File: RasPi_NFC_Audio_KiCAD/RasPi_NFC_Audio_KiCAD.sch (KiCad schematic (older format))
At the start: 21 parts, among them J1 Barrel_Jack_Switch, J2 Conn_02x20_Odd_Even, J3 Connector_01x10, U1 MIC5225-3.3V

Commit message: Layout updates
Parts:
- J2: footprint Connector_PinSocket_2.54mm:PinSocket_2x20_P2.54mm_Vertical -> Connector_PinHeader_2.54mm:PinHeader_2x20_P2.54mm_Vertical
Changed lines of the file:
@@
 EESchema Schematic File Version 4
 LIBS:RasPi_NFC_Audio_KiCAD-cache
-EELAYER 30 0
+EELAYER 29 0
 EELAYER END
 $Descr A4 11693 8268
@@
 F 0 "J2" H 4130 6450 50  0000 C CNN
 F 1 "Conn_02x20_Odd_Even" H 4140 6416 50  0001 C CNN
-F 2 "Connector_PinSocket_2.54mm:PinSocket_2x20_P2.54mm_Vertical" H -760 4440 50  0001 C CNN
+F 2 "Connector_PinHeader_2.54mm:PinHeader_2x20_P2.54mm_Vertical" H -760 4440 50  0001 C CNN
 F 3 "" H -760 4440 50  0001 C CNN
 F 4 "M20-7831046" H 4090 5390 50  0001 C CNN "Part #"

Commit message: Layout updates
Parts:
- added C28: 100u, Capacitor_SMD:C_1206_3216Metric_Pad1.42x1.75mm_HandSolder, symbol Device:C
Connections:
- net +5V: now also C28.1
- net GND: now also C28.2
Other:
- moved on the sheet: C1, C2, TP2
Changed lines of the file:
@@
 EESchema Schematic File Version 4
 LIBS:RasPi_NFC_Audio_KiCAD-cache
-EELAYER 29 0
+EELAYER 30 0
 EELAYER END
 $Descr A4 11693 8268
@@
 L Device:C C1
 U 1 1 5E1A86EE
-P 2060 2330
-F 0 "C1" H 2175 2376 50  0000 L CNN
-F 1 "100u" H 2175 2285 50  0000 L CNN
-F 2 "Capacitor_SMD:C_1206_3216Metric_Pad1.42x1.75mm_HandSolder" H 2098 2180 50  0001 C CNN
-F 3 "~" H 2060 2330 50  0001 C CNN
-F 4 "GRM31CD80J107ME39L" H 2060 2330 50  0001 C CNN "Part #"
-F 5 "490-10525-1-ND" H 2060 2330 50  0001 C CNN "DigiKey"
-	1    2060 2330
+P 1960 2330
+F 0 "C1" H 2000 2420 50  0000 L CNN
+F 1 "100u" H 1990 2230 50  0000 L CNN
+F 2 "Capacitor_SMD:C_1206_3216Metric_Pad1.42x1.75mm_HandSolder" H 1998 2180 50  0001 C CNN
+F 3 "~" H 1960 2330 50  0001 C CNN
+F 4 "GRM31CD80J107ME39L" H 1960 2330 50  0001 C CNN "Part #"
+F 5 "490-10525-1-ND" H 1960 2330 50  0001 C CNN "DigiKey"
+	1    1960 2330
 	1    0    0    -1
 $EndComp
@@
 L Device:C C2
 U 1 1 5E1AABBB
-P 2510 2330
-F 0 "C2" H 2625 2376 50  0000 L CNN
-F 1 "10u" H 2625 2285 50  0000 L CNN
-F 2 "Capacitor_SMD:C_0603_1608Metric_Pad1.05x0.95mm_HandSolder" H 2548 2180 50  0001 C CNN
-F 3 "~" H 2510 2330 50  0001 C CNN
-F 4 "CL10A106MQ8NNNC" H 2510 2330 50  0001 C CNN "Part #"
-F 5 "1276-1119-1-ND" H 2510 2330 50  0001 C CNN "DigiKey"
-	1    2510 2330
+P 2650 2330
+F 0 "C2" H 2680 2410 50  0000 L CNN
+F 1 "10u" H 2680 2240 50  0000 L CNN
+F 2 "Capacitor_SMD:C_0603_1608Metric_Pad1.05x0.95mm_HandSolder" H 2688 2180 50  0001 C CNN
+F 3 "~" H 2650 2330 50  0001 C CNN
+F 4 "CL10A106MQ8NNNC" H 2650 2330 50  0001 C CNN "Part #"
+F 5 "1276-1119-1-ND" H 2650 2330 50  0001 C CNN "DigiKey"
+	1    2650 2330
 	1    0    0    -1
 $EndComp
@@
 L power:GND #PWR0102
 U 1 1 5E1B33E8
-P 2060 2550
-F 0 "#PWR0102" H 2060 2300 50  0001 C CNN
-F 1 "GND" H 2060 2400 50  0000 C CNN
-F 2 "" H 2060 2550 50  0000 C CNN
-F 3 "" H 2060 2550 50  0000 C CNN
-	1    2060 2550
+P 1960 2550
+F 0 "#PWR0102" H 1960 2300 50  0001 C CNN
+F 1 "GND" H 1960 2400 50  0000 C CNN
+F 2 "" H 1960 2550 50  0000 C CNN
+F 3 "" H 1960 2550 50  0000 C CNN
+	1    1960 2550
 	1    0    0    -1
 $EndComp
@@
 L power:GND #PWR0103
 U 1 1 5E1B3827
-P 2510 2550
-F 0 "#PWR0103" H 2510 2300 50  0001 C CNN
-F 1 "GND" H 2510 2400 50  0000 C CNN
-F 2 "" H 2510 2550 50  0000 C CNN
-F 3 "" H 2510 2550 50  0000 C CNN
-	1    2510 2550
-	1    0    0    -1
-$EndComp
-Wire Wire Line
-	2060 2550 2060 2480
-Wire Wire Line
-	2510 2550 2510 2480
-Wire Wire Line
-	2060 2180 2060 2120
-Wire Wire Line
-	2510 2180 2510 2120
+P 2650 2550
+F 0 "#PWR0103" H 2650 2300 50  0001 C CNN
+F 1 "GND" H 2650 2400 50  0000 C CNN
+F 2 "" H 2650 2550 50  0000 C CNN
+F 3 "" H 2650 2550 50  0000 C CNN
+	1    2650 2550
+	1    0    0    -1
+$EndComp
+Wire Wire Line
+	1960 2550 1960 2480
+Wire Wire Line
+	2650 2550 2650 2480
+Wire Wire Line
+	2650 2180 2650 2120
 $Comp
 L power:GND #PWR0104
@@
 Wire Wire Line
 	2830 2120 2960 2120
-Connection ~ 2060 2120
-Wire Wire Line
-	2060 2120 2510 2120
-Connection ~ 2510 2120
-Wire Wire Line
-	2510 2120 2830 2120
+Connection ~ 2650 2120
 $Comp
 L power:+5V #PWR0106
 U 1 1 5E1C9964
-P 2060 1940
-F 0 "#PWR0106" H 2060 1790 50  0001 C CNN
-F 1 "+5V" H 2060 2080 50  0000 C CNN
-F 2 "" H 2060 1940 50  0000 C CNN
-F 3 "" H 2060 1940 50  0000 C CNN
-	1    2060 1940
+P 1960 1940
+F 0 "#PWR0106" H 1960 1790 50  0001 C CNN
+F 1 "+5V" H 1960 2080 50  0000 C CNN
+F 2 "" H 1960 1940 50  0000 C CNN
+F 3 "" H 1960 1940 50  0000 C CNN
+	1    1960 1940
 	1    0    0    -1
 $EndComp
@@
 $EndComp
 Wire Wire Line
-	2060 1940 2060 1980
+	1960 1940 1960 1980
 $Comp
 L power:VCOM #PWR0108
@@
 L Connector:TestPoint TP2
 U 1 1 5E2FD82C
-P 1970 1980
-F 0 "TP2" V 2050 2030 50  0000 L CNN
-F 1 "TestPoint" H 2028 2007 50  0001 L CNN
-F 2 "TestPoint:TestPoint_Keystone_5019_Minature" H 2170 1980 50  0001 C CNN
-F 3 "~" H 2170 1980 50  0001 C CNN
-	1    1970 1980
+P 1870 1980
+F 0 "TP2" V 1950 2030 50  0000 L CNN
+F 1 "TestPoint" H 1928 2007 50  0001 L CNN
+F 2 "TestPoint:TestPoint_Keystone_5019_Minature" H 2070 1980 50  0001 C CNN
+F 3 "~" H 2070 1980 50  0001 C CNN
+	1    1870 1980
 	0    -1   -1   0
 $EndComp
 Wire Wire Line
-	1730 2120 2060 2120
-Wire Wire Line
-	1970 1980 2060 1980
-Connection ~ 2060 1980
-Wire Wire Line
-	2060 1980 2060 2120
+	1730 2120 1960 2120
+Wire Wire Line
+	1870 1980 1960 1980
+Connection ~ 1960 1980
+Wire Wire Line
+	1960 1980 1960 2120
 $Comp
 L Connector:TestPoint TP1
@@
 Wire Wire Line
 	1600 1580 1600 1640
+Connection ~ 1960 2120
+Wire Wire Line
+	1960 2180 1960 2120
+Wire Wire Line
+	2650 2120 2830 2120
+Wire Wire Line
+	1960 2120 2300 2120
+$Comp
+L Device:C C28
+U 1 1 5E23A078
+P 2300 2330
+F 0 "C28" H 2340 2420 50  0000 L CNN
+F 1 "100u" H 2330 2230 50  0000 L CNN
+F 2 "Capacitor_SMD:C_1206_3216Metric_Pad1.42x1.75mm_HandSolder" H 2338 2180 50  0001 C CNN
+F 3 "~" H 2300 2330 50  0001 C CNN
+F 4 "GRM31CD80J107ME39L" H 2300 2330 50  0001 C CNN "Part #"
+F 5 "490-10525-1-ND" H 2300 2330 50  0001 C CNN "DigiKey"
+	1    2300 2330
+	1    0    0    -1
+$EndComp
+$Comp
+L power:GND #PWR06
+U 1 1 5E23A7C7
+P 2300 2550
+F 0 "#PWR06" H 2300 2300 50  0001 C CNN
+F 1 "GND" H 2300 2400 50  0000 C CNN
+F 2 "" H 2300 2550 50  0000 C CNN
+F 3 "" H 2300 2550 50  0000 C CNN
+	1    2300 2550
+	1    0    0    -1
+$EndComp
+Wire Wire Line
+	2300 2550 2300 2480
+Wire Wire Line
+	2300 2180 2300 2120
+Connection ~ 2300 2120
+Wire Wire Line
+	2300 2120 2650 2120
 $EndSCHEMATC

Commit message: Layout updates
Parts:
- removed J3: Connector_01x10, Connector_PinHeader_2.54mm:PinHeader_1x10_P2.54mm_Vertical, symbol Connector_Generic:Conn_01x10
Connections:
- no-connect marks 18 -> 17
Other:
- note removed: "Debug Header"
- moved on the sheet: C1, C2, C28, C3, C4, C5, J1, J2, MK1, MK2, MK3, MK4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

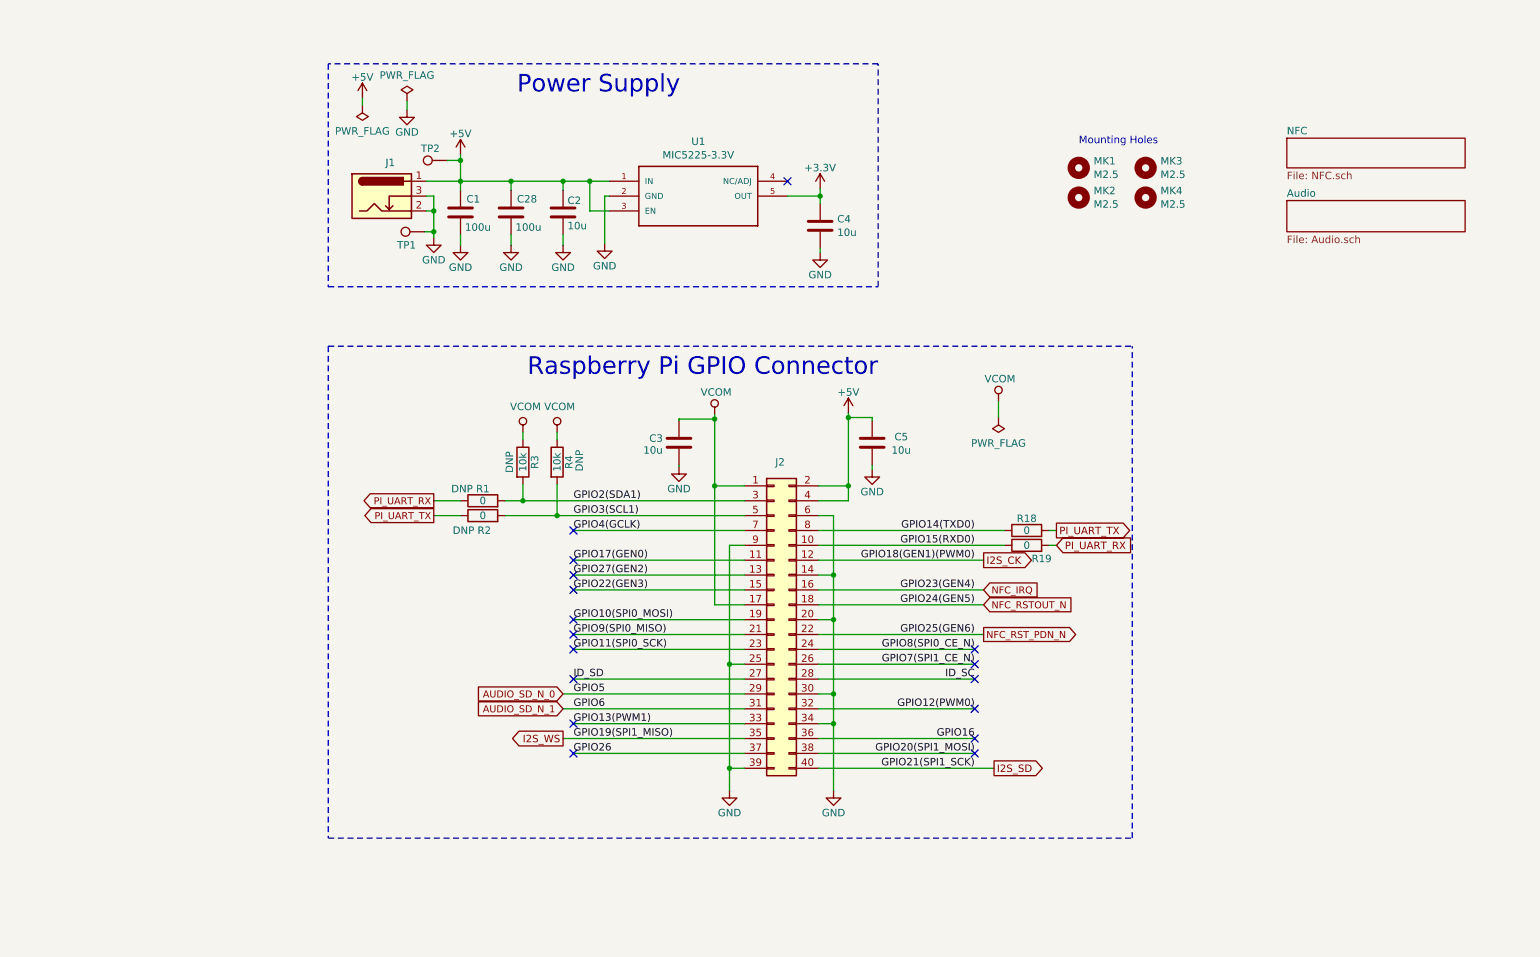
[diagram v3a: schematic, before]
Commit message: Added GPIO expander to schematic
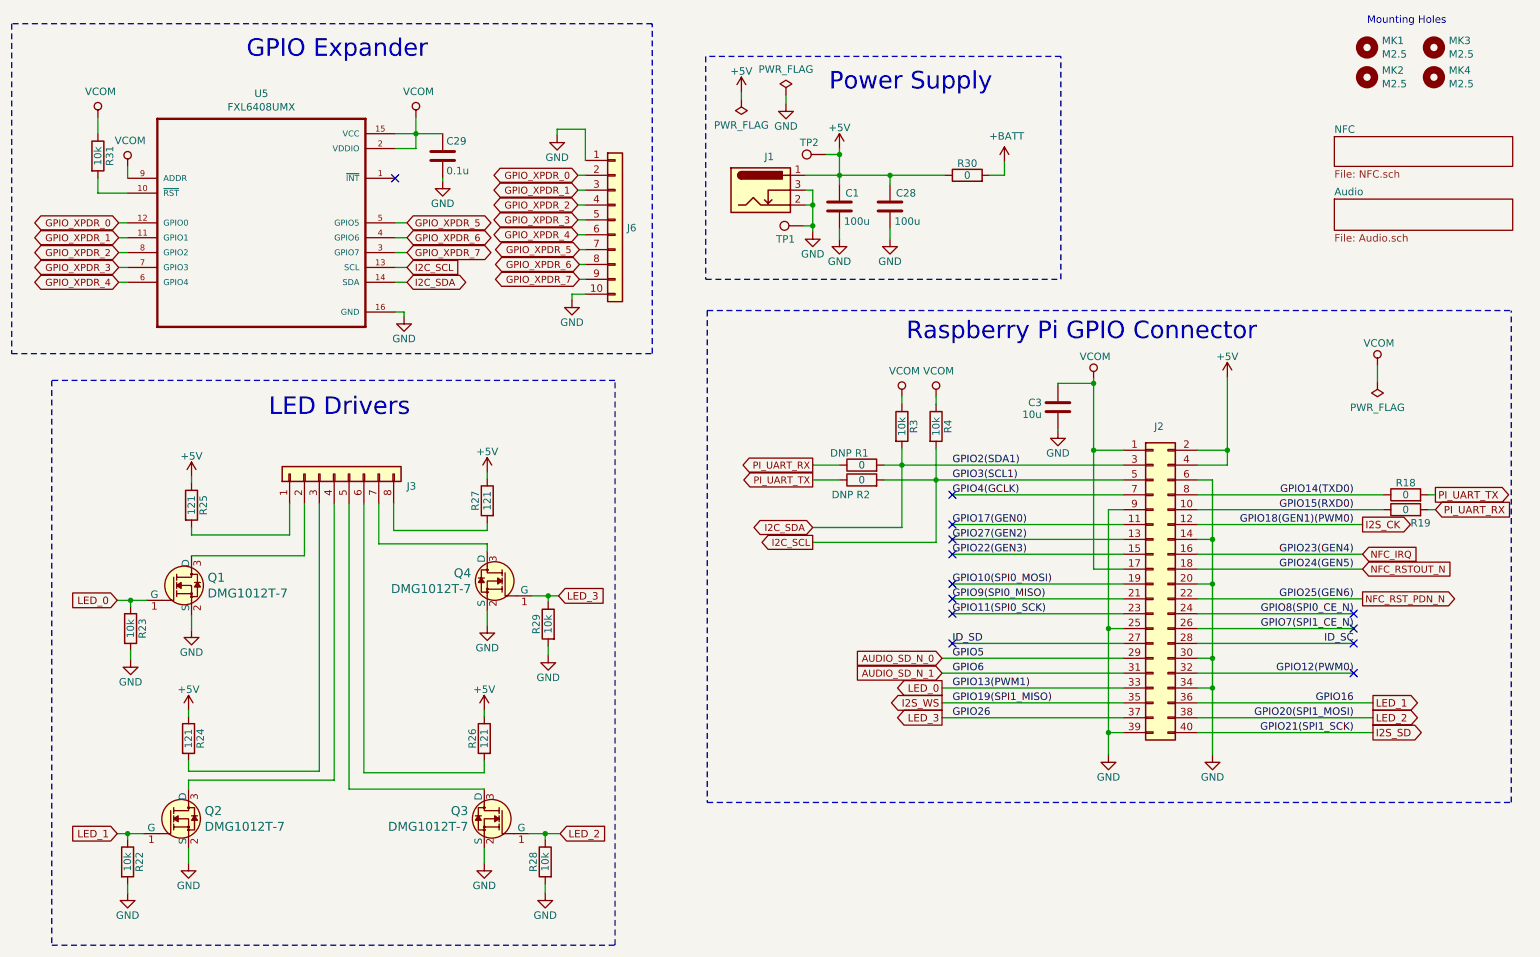
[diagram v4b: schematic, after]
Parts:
- removed C2, C4, C5: 10u, Capacitor_SMD:C_0603_1608Metric_Pad1.05x0.95mm_HandSolder, symbol Device:C
- removed U1: MIC5225-3.3V, Package_TO_SOT_SMD:SOT-23-5, symbol MIC5225:MIC5225
- added C29: 0.1u, Capacitor_SMD:C_0603_1608Metric_Pad1.05x0.95mm_HandSolder, symbol Device:C
- added J3: Conn_01x08, Connector_PinHeader_2.54mm:PinHeader_1x08_P2.54mm_Horizontal, symbol Connector_Generic:Conn_01x08
- added J6: Conn_01x10, symbol Connector_Generic:Conn_01x10
- added Q1, Q2, Q3, Q4: DMG1012T-7, digikey-footprints:SOT-523, symbol dk_Transistors-FETs-MOSFETs-Single:DMG1012T-7
- added R22, R23, R28, R29, R31: 10k, Resistor_SMD:R_0603_1608Metric_Pad1.05x0.95mm_HandSolder, symbol Device:R
- added R24, R25, R26, R27: 121, Resistor_SMD:R_0603_1608Metric_Pad1.05x0.95mm_HandSolder, symbol Device:R
- added R30: 0, Resistor_SMD:R_0603_1608Metric_Pad1.05x0.95mm_HandSolder, symbol Device:R
- added U5: FXL6408UMX, QFN40P260X180X55-16N, symbol FXL6408UMX:FXL6408UMX
- R3, R4: DNP DNP -> (none)
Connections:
- net +5V: now also R24.1, R25.1, R26.1, R27.1, R30.1
- net GND: now also C29.2, J6.1 (Pin_1), J6.10 (Pin_10), Q1.2 (S), Q2.2 (S), Q3.2 (S), Q4.2 (S), R22.2, R23.2, R28.2, R29.2, U5.16 (GND)
- net VCOM: now also C29.1, R31.1, U5.15 (VCC), U5.2 (VDDIO), U5.9 (ADDR)
- net GPIO13(PWM1) renamed LED_0
- net LED_0: now also Q1.1 (G), R23.1
- net GPIO16 renamed LED_1
- net LED_1: now also Q2.1 (G), R22.1
- net GPIO2(SDA1) renamed I2C_SDA
- net I2C_SDA: now also U5.14 (SDA)
- net GPIO20(SPI1_MOSI) renamed LED_2
- net LED_2: now also Q3.1 (G), R28.1
- net GPIO26 renamed LED_3
- net LED_3: now also Q4.1 (G), R29.1
- net GPIO3(SCL1) renamed I2C_SCL
- net I2C_SCL: now also U5.13 (SCL)
- new net: J3.4 (Pin_4), Q2.3 (D)
- new net: J3.3 (Pin_3), R24.2
- new net: J3.7 (Pin_7), Q4.3 (D)
- new net: J3.8 (Pin_8), R27.2
- new net: J3.5 (Pin_5), Q3.3 (D)
- new net: J3.6 (Pin_6), R26.2
- new net: J3.2 (Pin_2), Q1.3 (D)
- new net: J3.1 (Pin_1), R25.2
- new net: R31.2, U5.10 (~RST~)
- new net +BATT: R30.2
- new net GPIO_XPDR_0: J6.2 (Pin_2), U5.12 (GPIO0)
- new net GPIO_XPDR_1: J6.3 (Pin_3), U5.11 (GPIO1)
- new net GPIO_XPDR_2: J6.4 (Pin_4), U5.8 (GPIO2)
- new net GPIO_XPDR_3: J6.5 (Pin_5), U5.7 (GPIO3)
- new net GPIO_XPDR_4: J6.6 (Pin_6), U5.6 (GPIO4)
- new net GPIO_XPDR_5: J6.7 (Pin_7), U5.5 (GPIO5)
- new net GPIO_XPDR_6: J6.8 (Pin_8), U5.4 (GPIO6)
- new net GPIO_XPDR_7: J6.9 (Pin_9), U5.3 (GPIO7)
- no-connect marks 17 -> 13
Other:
- note added: "GPIO Expander"
- note added: "LED Drivers"
- moved on the sheet: C1, C28, C3, J1, J2, MK1, MK2, MK3, MK4, R1, R18, R19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

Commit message: Updated layout for GPIO expander
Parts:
- J3: DigiKey (none) -> 952-2249-ND; Part # (none) -> M20-9960845
- J6: footprint (none) -> Connector_PinHeader_2.54mm:PinHeader_1x10_P2.54mm_Horizontal; DigiKey (none) -> 609-3322-ND; Part # (none) -> 68016-210HLF
- Q1, Q2, Q3, Q4: footprint digikey-footprints:SOT-523 -> RasPi_NFC_Audio_PCB_Lib:SOT-523; DigiKey (none) -> DMG1012T-7DICT-ND; Part # (none) -> DMG1012T-7
- U5: footprint QFN40P260X180X55-16N -> RasPi_NFC_Audio_PCB_Lib:QFN40P260X180X55-16N; DigiKey (none) -> FXL6408UMXCT-ND; Part # (none) -> FXL6408UMX
